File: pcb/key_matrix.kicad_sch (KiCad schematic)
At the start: 159 parts, among them K000 1.5U, K001 1U, K002 1U, K003 1U, K004 1U, K005 1U, K006 1U, K007 1U, K008 1U, K009 1U, K010 1U, K011 1U, K012 1U, K013 1.5U, K100 1.5U, K101 1U, K102 1U, K103 1U, K104 1U, K105 1U, K106 1U, K107 1U, K108 1U, K109 1U, K110 1U, K111 1U, K112 1U, K113 1.5U, K200 1.5U, K201 1U, K202 1U, K203 1U, K204 1U, K205 1U, K206 1U, K207 1U, K208 1U, K209 1U, K210 1U, K211 1U, K212 1U, K213 1.5U, K300 1.5U, K301 1U, K302 1U, K303 1U, K304 1U, K305 1U, K306 1U, K307 1U, K308 1U, K309 1U, K310 1U, K311 1U, K312 1U, K313 1.5U, K400 1.5U, K401 1U, K402 1U, K403 1U, K404 1U, K405 1U, K406 1U, K407 1U, K408 1U, K409 1U, K410 1U, K411 1U, K412 1U, K413 1.5U, U3 IS31FL3731-QF

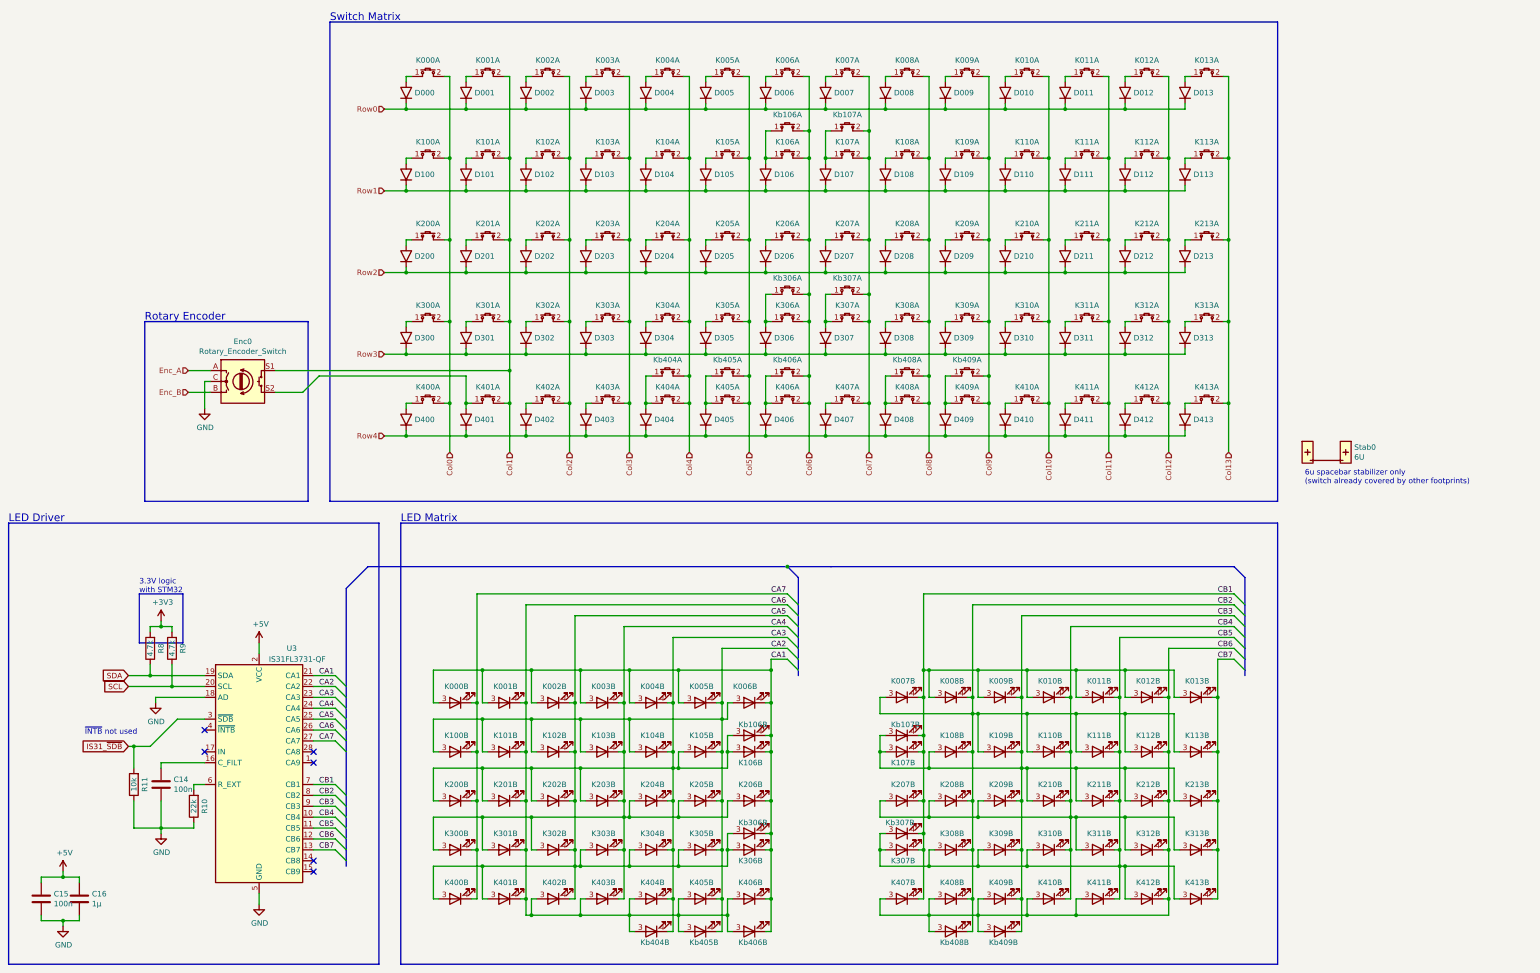
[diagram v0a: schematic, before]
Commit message: Switched to RP2040 - PCB finalization
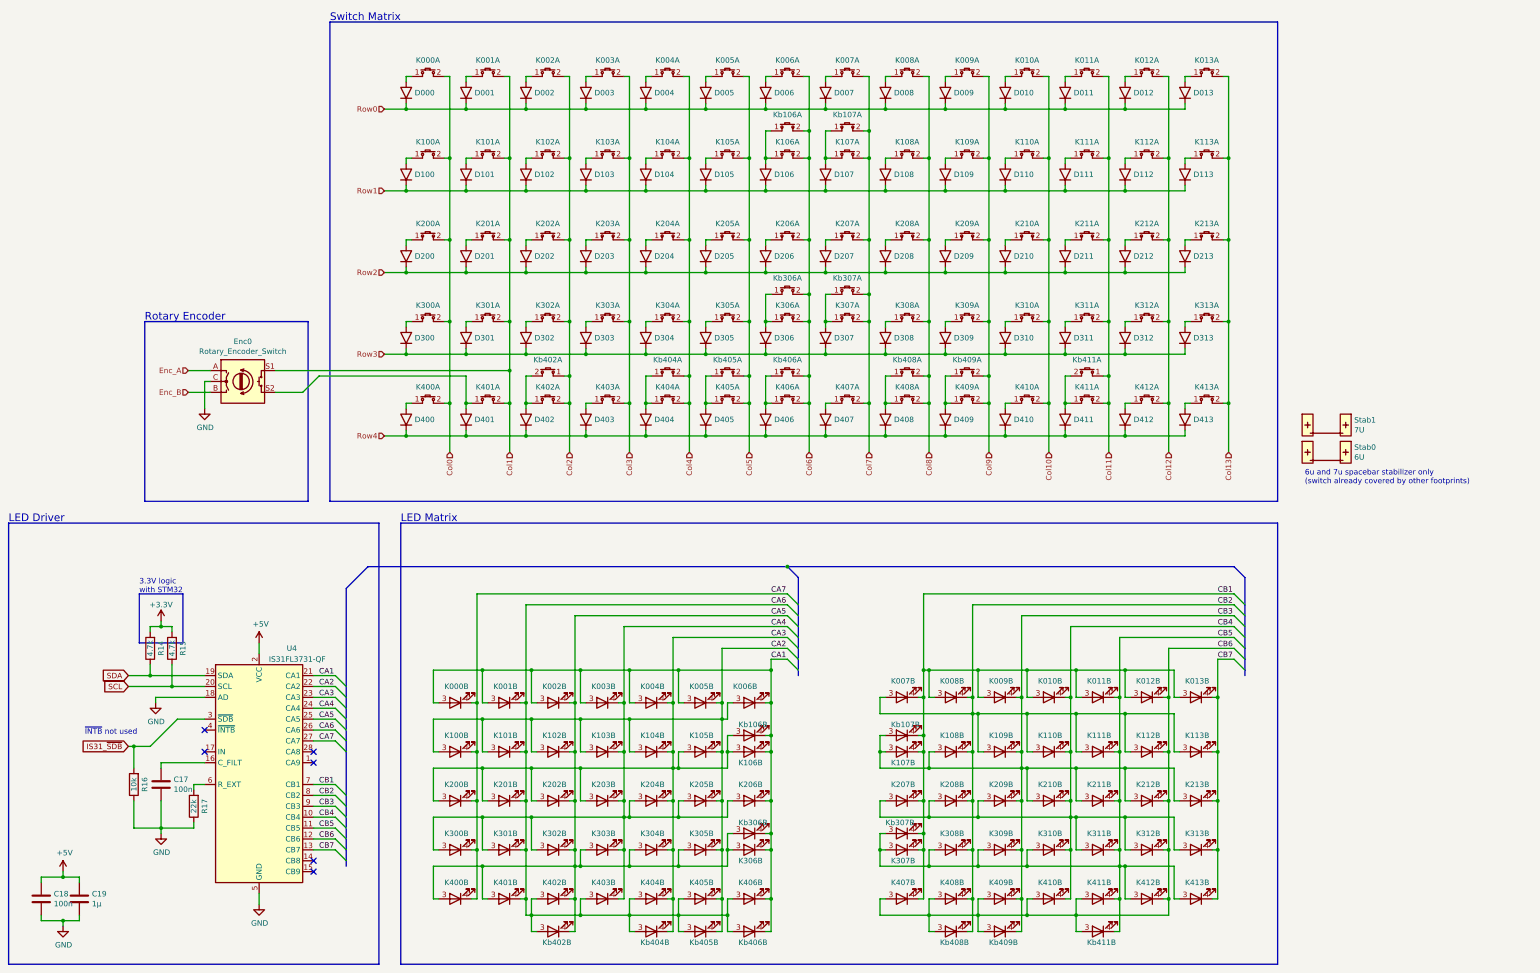
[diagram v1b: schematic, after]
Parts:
- added Kb402, Kb411: 1.5U, 0xLib_MK_Switches:MXOnly-1.5U-Flipped, symbol 0xLib_MK:Key_Switch_LED
- added Stab1: 7U, 0xLib_MK_Switches:MXOnly-7U-ReversedStabilizersOnly, symbol 0xLib_MK:Stabilizer
- C17: renamed from C14; LCSC (none) -> C14663
- C18: renamed from C15; LCSC (none) -> C14663
- C19: renamed from C16; LCSC (none) -> C15849
- D000, D001, D002, D003, D004, D005, D006, D007, D008, D009, D010, D011, D012, D013, D100, D101, D102, D103, D104, D105, D106, D107, D108, D109, D110, D111, D112, D113, D200, D201, D202, D203, D204, D205, D206, D207, D208, D209, D210, D211, D212, D213, D300, D301, D302, D303, D304, D305, D306, D307, D308, D309, D310, D311, D312, D313, D400, D401, D402, D403, D404, D405, D406, D407, D408, D409, D410, D411, D412, D413: FancyRef %true% -> (none); LCSC (none) -> C2128
- Enc0: symbol Device:Rotary_Encoder_Switch -> Device:RotaryEncoder_Switch; now left out of the parts list
- K000, K001, K002, K003, K004, K005, K006, K007, K008, K009, K010, K011, K012, K013, K100, K101, K102, K103, K104, K105, K106, K107, K108, K109, K110, K111, K112, K113, K200, K201, K202, K203, K204, K205, K206, K207, K208, K209, K210, K211, K212, K213, K300, K301, K302, K303, K304, K305, K306, K307, K308, K309, K310, K311, K312, K313, K400, K401, K402, K403, K404, K405, K406, K407, K408, K409, K410, K411, K412, K413, Kb106, Kb107, Kb306, Kb307, Kb404, Kb405, Kb406, Kb408, Kb409: FancyRef %true% -> (none)
- R14: renamed from R8; LCSC (none) -> C23162
- R15: renamed from R9; LCSC (none) -> C23162
- R16: renamed from R11; LCSC (none) -> C25804
- R17: renamed from R10; LCSC (none) -> C31850
- Stab0: now left out of the parts list
- U4: renamed from U3; LCSC (none) -> C191206
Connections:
- net CA5: now also Kb402.4 (K)
- net CA6: now also Kb402.3 (A)
- net CB5: now also Kb411.4 (K)
- net CB6: now also Kb411.3 (A)
- net Col11: now also Kb411.1
- net Col2: now also Kb402.1
- net at D402.2 (A), K402.1: now also Kb402.2
- net at D411.2 (A), K411.1: now also Kb411.2
- net +3V3 renamed +3.3V
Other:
- note added: "6u and 7u spacebar stabilizer only (switch already covered by other footprints)"
- note removed: "6u spacebar stabilizer only (switch already covered by other footprints)"
